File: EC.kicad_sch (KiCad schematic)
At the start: 9 parts, among them CN1 BM04B-SRSS-TB(LF)(SN), CN2 B4B-ZR (LF)(SN), CN3 ZH1.5-6P-LT, J1 Conn_01x06_Socket, J2 Conn_02x05_Odd_Even, J3 Conn_02x05_Odd_Even, U13 B6B-ZR (LF)(SN), U2 B5B-ZR-(LF)(SN)

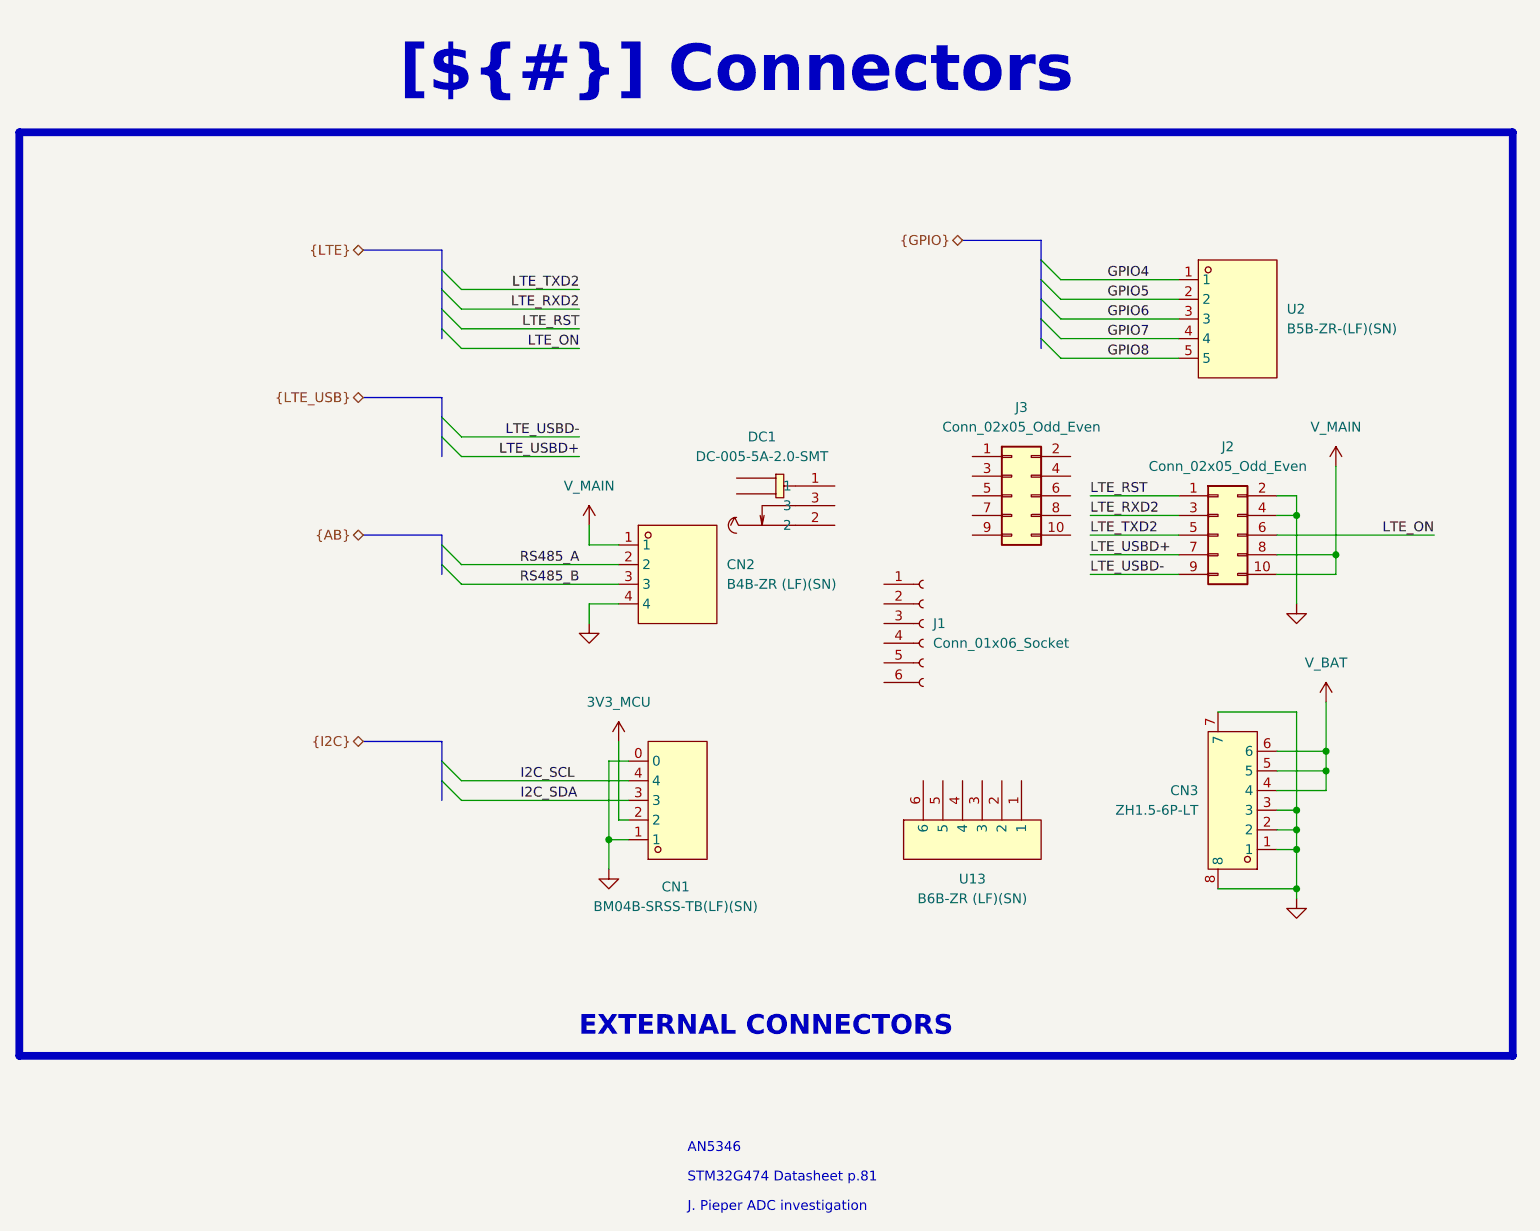
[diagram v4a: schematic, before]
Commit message: [Schematic/PCB][Added] Connectors, layout, preliminar routing
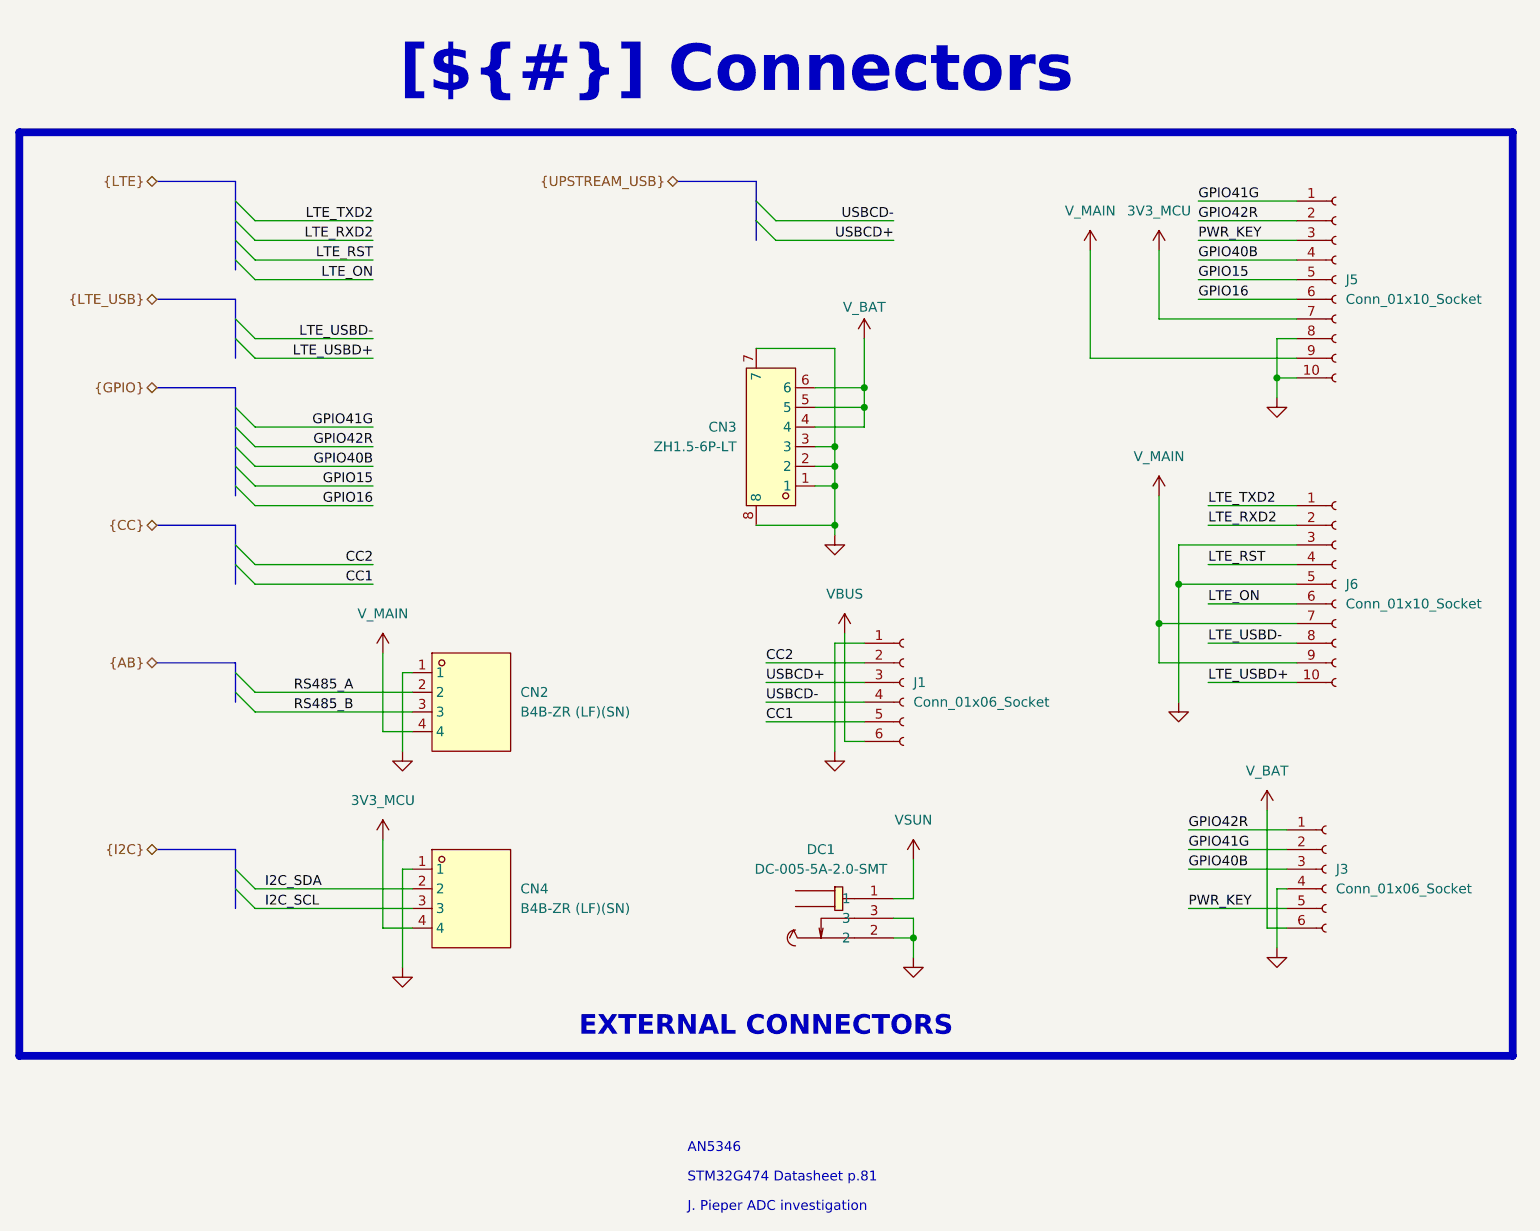
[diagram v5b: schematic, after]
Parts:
- removed CN1: BM04B-SRSS-TB(LF)(SN), easyeda2kicad:CONN-SMD_BM04B-SRSS-TB, symbol easyeda2kicad:BM04B-SRSS-TB(LF)(SN)
- removed J2: Conn_02x05_Odd_Even, Connector_PinHeader_2.54mm:PinHeader_2x05_P2.54mm_Horizontal, symbol Connector_Generic:Conn_02x05_Odd_Even
- removed J3: Conn_02x05_Odd_Even, Connector_PinHeader_2.54mm:PinHeader_2x05_P2.54mm_Vertical, symbol Connector_Generic:Conn_02x05_Odd_Even
- removed U13: B6B-ZR (LF)(SN), easyeda2kicad:CONN-TH-6P-P1.50_B6B-ZR-LF-SN, symbol easyeda2kicad:B6B-ZR(LF)(SN)
- removed U2: B5B-ZR-(LF)(SN), easyeda2kicad:CONN-TH_5P-P1.50_B5B-ZR-LF-SN, symbol easyeda2kicad:B5B-ZR-(LF)(SN)
- added CN4: B4B-ZR (LF)(SN), easyeda2kicad:CONN-TH_B4B-ZR-LF-SN, symbol easyeda2kicad:B4B-ZR(LF)(SN)
- added J3: Conn_01x06_Socket, Connector_JST:JST_ZH_B6B-ZR_1x06_P1.50mm_Vertical, symbol Connector:Conn_01x06_Socket
- added J5, J6: Conn_01x10_Socket, Connector_PinHeader_2.54mm:PinHeader_2x05_P2.54mm_Vertical, symbol Connector:Conn_01x10_Socket
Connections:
- net 3V3_MCU: now also CN4.4, J5.7 (Pin_7)
- net GND: now also CN2.1, DC1.2, DC1.3, J1.1 (Pin_1), CN4.1, J3.4 (Pin_4), J5.10 (Pin_10), J5.8 (Pin_8), J6.3 (Pin_3), J6.5 (Pin_5); no longer CN2.4
- net I2C_SCL: now also CN4.3
- net I2C_SDA: now also CN4.2
- net LTE_ON: now also J6.6 (Pin_6)
- net LTE_RST: now also J6.4 (Pin_4)
- net LTE_RXD2: now also J6.2 (Pin_2)
- net LTE_TXD2: now also J6.1 (Pin_1)
- net LTE_USBD+: now also J6.10 (Pin_10)
- net LTE_USBD-: now also J6.8 (Pin_8)
- net V_BAT: now also J3.6 (Pin_6)
- net V_MAIN: now also CN2.4, J5.9 (Pin_9), J6.7 (Pin_7), J6.9 (Pin_9); no longer CN2.1
- net VSUN: now reaches DC1.1
- net CC2: now reaches J1.2 (Pin_2)
- net USBCD+: now reaches J1.3 (Pin_3)
- net USBCD-: now reaches J1.4 (Pin_4)
- net CC1: now reaches J1.5 (Pin_5)
- net VBUS: now reaches J1.6 (Pin_6)
- new net GPIO15: J5.5 (Pin_5)
- new net GPIO16: J5.6 (Pin_6)
- new net GPIO40B: J3.3 (Pin_3), J5.4 (Pin_4)
- new net GPIO41G: J3.2 (Pin_2), J5.1 (Pin_1)
- new net GPIO42R: J3.1 (Pin_1), J5.2 (Pin_2)
- new net PWR_KEY: J3.5 (Pin_5), J5.3 (Pin_3)
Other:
- moved on the sheet: CN2, CN3, DC1, J1

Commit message: [Schematic/PCB][Added] Routing almost finished
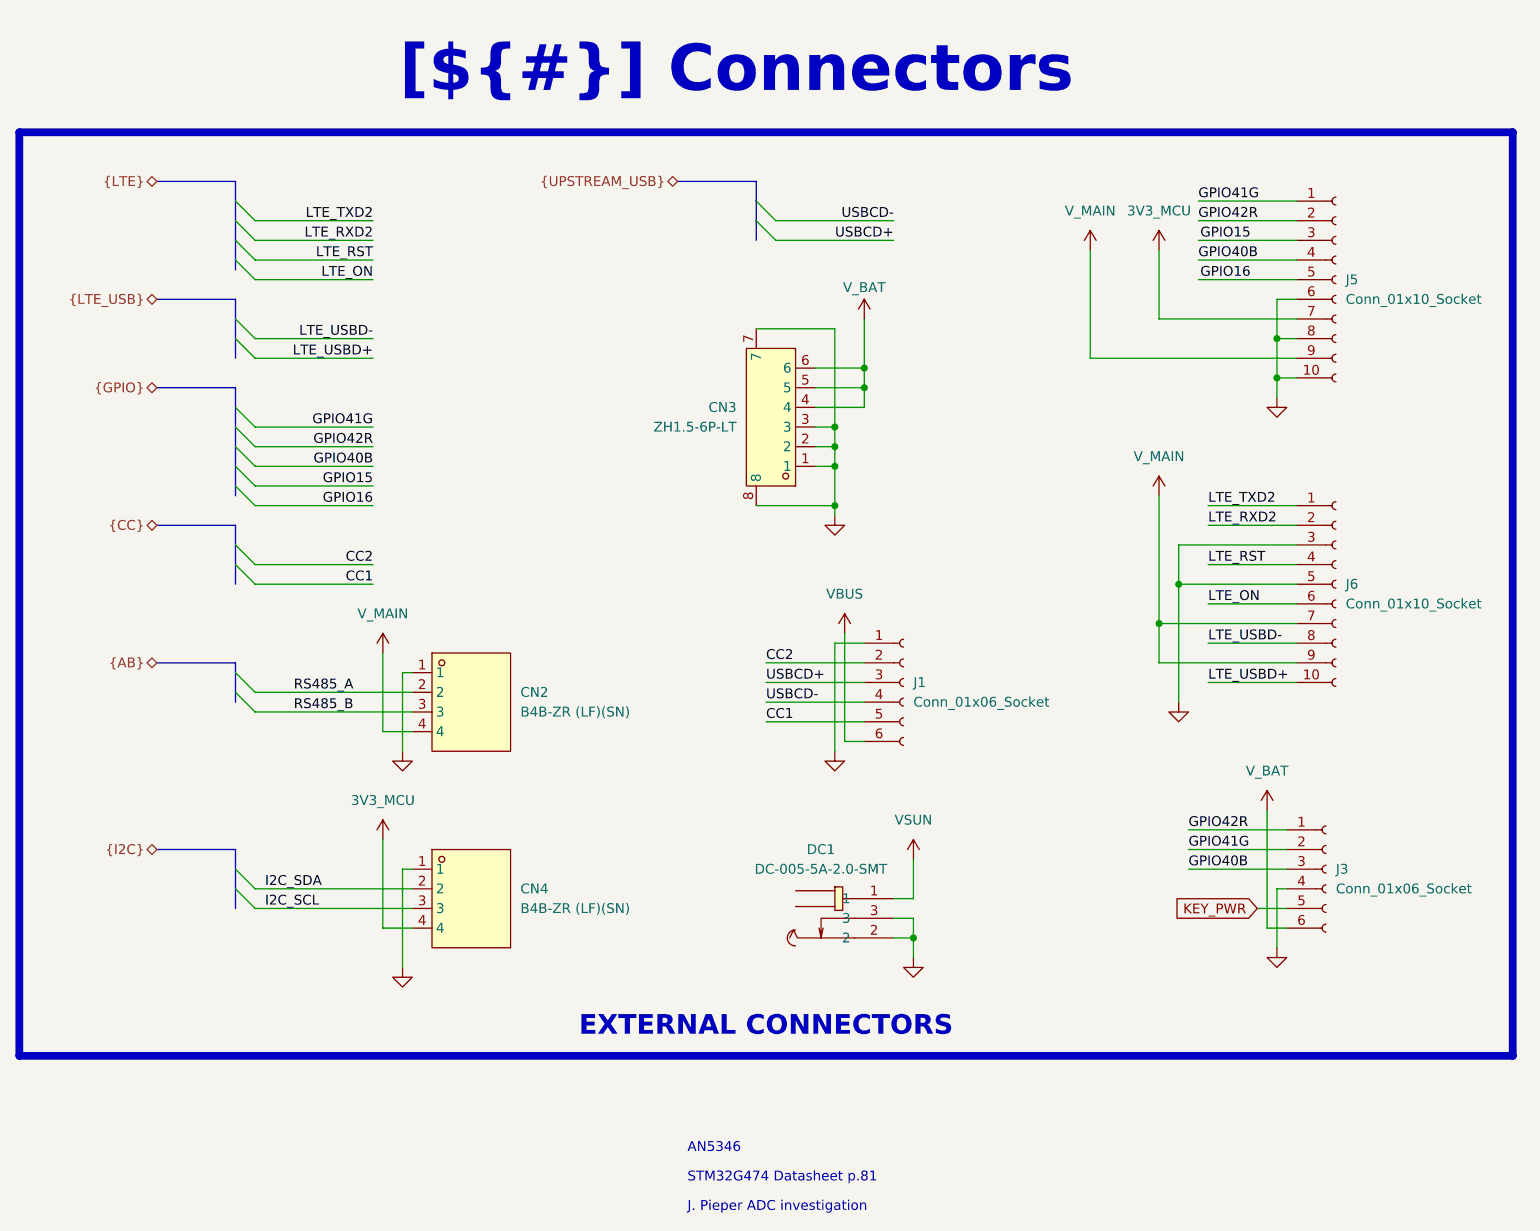
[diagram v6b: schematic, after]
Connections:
- net GND: now also J5.6 (Pin_6)
- net GPIO15: now also J5.3 (Pin_3); no longer J5.5 (Pin_5)
- net GPIO16: now also J5.5 (Pin_5); no longer J5.6 (Pin_6)
- net PWR_KEY renamed KEY_PWR
- net KEY_PWR: no longer J5.3 (Pin_3)
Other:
- moved on the sheet: CN3
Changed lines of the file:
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@@
 	)
 	(junction
-		(at 161.29 73.66)
+		(at 161.29 71.12)
 		(diameter 0)
 		(color 0 0 0 0)
@@
 	)
 	(junction
-		(at 165.1 66.04)
+		(at 165.1 63.5)
 		(diameter 0)
 		(color 0 0 0 0)
 	)
 	(junction
-		(at 165.1 63.5)
+		(at 165.1 60.96)
 		(diameter 0)
 		(color 0 0 0 0)
@@
 	)
 	(junction
-		(at 161.29 76.2)
+		(at 161.29 73.66)
 		(diameter 0)
 		(color 0 0 0 0)
 	)
 	(junction
-		(at 161.29 71.12)
+		(at 161.29 68.58)
 		(diameter 0)
 		(color 0 0 0 0)
 	)
 	(junction
-		(at 161.29 81.28)
+		(at 161.29 78.74)
+		(diameter 0)
+		(color 0 0 0 0)
+	)
+	(junction
+		(at 218.44 57.15)
 		(diameter 0)
 		(color 0 0 0 0)
@@
 	(wire
 		(pts
-			(xy 161.29 76.2) (xy 161.29 81.28)
+			(xy 161.29 73.66) (xy 161.29 78.74)
 		)
 		(stroke
@@
 	(wire
 		(pts
-			(xy 161.29 58.42) (xy 161.29 71.12)
+			(xy 161.29 55.88) (xy 161.29 68.58)
 		)
 		(stroke
@@
 	(wire
 		(pts
-			(xy 207.01 130.81) (xy 219.71 130.81)
+			(xy 215.9 130.81) (xy 219.71 130.81)
 		)
 		(stroke
@@
 	(wire
 		(pts
-			(xy 151.13 81.28) (xy 161.29 81.28)
+			(xy 151.13 78.74) (xy 161.29 78.74)
 		)
 		(stroke
@@
 	(wire
 		(pts
-			(xy 158.75 76.2) (xy 161.29 76.2)
+			(xy 158.75 73.66) (xy 161.29 73.66)
 		)
 		(stroke
@@
 		)
 	)
+	(wire
+		(pts
+			(xy 218.44 52.07) (xy 218.44 57.15)
+		)
+		(stroke
+			(width 0)
+			(type default)
+		)
+	)
 	(bus
 		(pts
@@
 	(wire
 		(pts
+			(xy 208.28 44.45) (xy 220.98 44.45)
+		)
+		(stroke
+			(width 0)
+			(type default)
+		)
+	)
+	(wire
+		(pts
 			(xy 220.98 57.15) (xy 218.44 57.15)
 		)
@@
 	(wire
 		(pts
-			(xy 158.75 73.66) (xy 161.29 73.66)
+			(xy 158.75 71.12) (xy 161.29 71.12)
 		)
 		(stroke
@@
 	(wire
 		(pts
-			(xy 161.29 73.66) (xy 161.29 76.2)
+			(xy 161.29 71.12) (xy 161.29 73.66)
 		)
 		(stroke
@@
 	(wire
 		(pts
-			(xy 208.28 44.45) (xy 220.98 44.45)
-		)
-		(stroke
-			(width 0)
-			(type default)
-		)
-	)
-	(wire
-		(pts
 			(xy 168.91 44.45) (xy 153.67 44.45)
 		)
@@
 	(wire
 		(pts
-			(xy 161.29 81.28) (xy 161.29 82.55)
+			(xy 161.29 78.74) (xy 161.29 80.01)
 		)
 		(stroke
@@
 	(wire
 		(pts
-			(xy 158.75 66.04) (xy 165.1 66.04)
-		)
-		(stroke
-			(width 0)
-			(type default)
-		)
-	)
-	(wire
-		(pts
-			(xy 208.28 52.07) (xy 220.98 52.07)
+			(xy 158.75 63.5) (xy 165.1 63.5)
 		)
 		(stroke
@@
 	(wire
 		(pts
-			(xy 165.1 66.04) (xy 165.1 63.5)
+			(xy 165.1 63.5) (xy 165.1 60.96)
 		)
 		(stroke
@@
 	(wire
 		(pts
-			(xy 161.29 71.12) (xy 161.29 73.66)
+			(xy 161.29 68.58) (xy 161.29 71.12)
 		)
 		(stroke
@@
 	(wire
 		(pts
-			(xy 151.13 58.42) (xy 161.29 58.42)
+			(xy 151.13 55.88) (xy 161.29 55.88)
 		)
 		(stroke
@@
 	(wire
 		(pts
+			(xy 220.98 52.07) (xy 218.44 52.07)
+		)
+		(stroke
+			(width 0)
+			(type default)
+		)
+	)
+	(wire
+		(pts
 			(xy 101.6 88.9) (xy 86.36 88.9)
 		)
@@
 	(wire
 		(pts
-			(xy 165.1 57.15) (xy 165.1 63.5)
+			(xy 165.1 54.61) (xy 165.1 60.96)
 		)
 		(stroke
@@
 	(wire
 		(pts
-			(xy 165.1 68.58) (xy 165.1 66.04)
+			(xy 165.1 66.04) (xy 165.1 63.5)
 		)
 		(stroke
@@
 	(wire
 		(pts
-			(xy 158.75 71.12) (xy 161.29 71.12)
+			(xy 158.75 68.58) (xy 161.29 68.58)
 		)
 		(stroke
@@
 	(wire
 		(pts
-			(xy 158.75 68.58) (xy 165.1 68.58)
+			(xy 158.75 66.04) (xy 165.1 66.04)
 		)
 		(stroke
@@
 	(wire
 		(pts
-			(xy 165.1 63.5) (xy 158.75 63.5)
+			(xy 165.1 60.96) (xy 158.75 60.96)
 		)
 		(stroke
@@
 		)
 	)
-	(label "GPIO16"
-		(at 208.28 52.07 0)
+	(label "GPIO15"
+		(at 208.534 44.45 0)
 		(effects
 			(font
@@
 		)
 	)
-	(label "GPIO15"
-		(at 208.28 49.53 0)
+	(label "GPIO16"
+		(at 208.534 49.53 0)
 		(effects
 			(font
@@
 		)
 	)
-	(label "PWR_KEY"
-		(at 208.28 44.45 0)
-		(effects
-			(font
-				(size 1.27 1.27)
-			)
-			(justify left bottom)
-		)
-	)
 	(label "LTE_RXD2"
 		(at 101.6 44.45 180)
@@
 		)
 	)
-	(label "PWR_KEY"
-		(at 207.01 130.81 0)
+	(global_label "KEY_PWR"
+		(shape input)
+		(at 215.9 130.81 180)
+		(fields_autoplaced yes)
 		(effects
 			(font
 				(size 1.27 1.27)
 			)
-			(justify left bottom)
+			(justify right)
+		)
+		(property "Intersheetrefs" "${INTERSHEET_REFS}"
+			(at 204.4482 130.81 0)
+			(effects
+				(font
+					(size 1.27 1.27)
+				)
+				(justify right)
+				(hide yes)
+			)
 		)
 	)
@@
 	(symbol
 		(lib_id "easyeda2kicad:ZH1.5-6P-LT")
-		(at 154.94 69.85 180)
+		(at 154.94 67.31 180)
 		(unit 1)
 		(exclude_from_sim no)
@@
 		(fields_autoplaced yes)
 		(property "Reference" "CN3"
-			(at 148.59 68.5799 0)
+			(at 148.59 66.0399 0)
 			(effects
 				(font
@@
 		)
 		(property "Value" "ZH1.5-6P-LT"
-			(at 148.59 71.1199 0)
+			(at 148.59 68.5799 0)
 			(effects
 				(font
@@
 		)
 		(property "Footprint" "easyeda2kicad:CONN-SMD_ZH1.5-6P-LT"
-			(at 154.94 50.8 0)
+			(at 154.94 48.26 0)
 			(effects
 				(font
@@
 		)
 		(property "Datasheet" "https://lcsc.com/product-detail/Wire-To-Board-Wire-To-Wire-Connector_CAX-ZH1-5-6P-LT_C722928.html"
-			(at 154.94 48.26 0)
+			(at 154.94 45.72 0)
 			(effects
 				(font
@@
 		)
 		(property "Description" ""
-			(at 154.94 69.85 0)
+			(at 154.94 67.31 0)
 			(effects
 				(font
@@
 		)
 		(property "LCSC Part" "C722928"
-			(at 154.94 45.72 0)
+			(at 154.94 43.18 0)
 			(effects
 				(font
@@
 	(symbol
 		(lib_id "power:GND")
-		(at 161.29 82.55 0)
+		(at 161.29 80.01 0)
 		(unit 1)
 		(exclude_from_sim no)
@@
 		(fields_autoplaced yes)
 		(property "Reference" "#PWR031"
-			(at 161.29 88.9 0)
+			(at 161.29 86.36 0)
 			(effects
 				(font
@@
 		)
 		(property "Value" "GND"
-			(at 161.29 87.63 0)
+			(at 161.29 85.09 0)
 			(effects
 				(font
@@
 		)
 		(property "Footprint" ""
-			(at 161.29 82.55 0)
+			(at 161.29 80.01 0)
 			(effects
 				(font
@@
 		)
 		(property "Datasheet" ""
-			(at 161.29 82.55 0)
+			(at 161.29 80.01 0)
 			(effects
 				(font
@@
 		)
 		(property "Description" "Power symbol creates a global label with name \"GND\" , ground"
-			(at 161.29 82.55 0)
+			(at 161.29 80.01 0)
 			(effects
 				(font
@@
 	(symbol
 		(lib_id "power:VCC")
-		(at 165.1 57.15 0)
+		(at 165.1 54.61 0)
 		(unit 1)
 		(exclude_from_sim no)
@@
 		(dnp no)
 		(property "Reference" "#PWR032"
-			(at 165.1 60.96 0)
+			(at 165.1 58.42 0)
 			(effects
 				(font
@@
 		)
 		(property "Value" "V_BAT"
-			(at 165.1 53.086 0)
+			(at 165.1 50.546 0)
 			(effects
 				(font
@@
 		)
 		(property "Footprint" ""
-			(at 165.1 57.15 0)
+			(at 165.1 54.61 0)
 			(effects
 				(font
@@
 		)
 		(property "Datasheet" ""
-			(at 165.1 57.15 0)
+			(at 165.1 54.61 0)
 			(effects
 				(font
@@
 		)
 		(property "Description" "Power symbol creates a global label with name \"VCC\""
-			(at 165.1 57.15 0)
+			(at 165.1 54.61 0)
 			(effects
 				(font
